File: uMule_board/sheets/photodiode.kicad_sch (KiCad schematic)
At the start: 1 part, among them U1 OPA330xxD

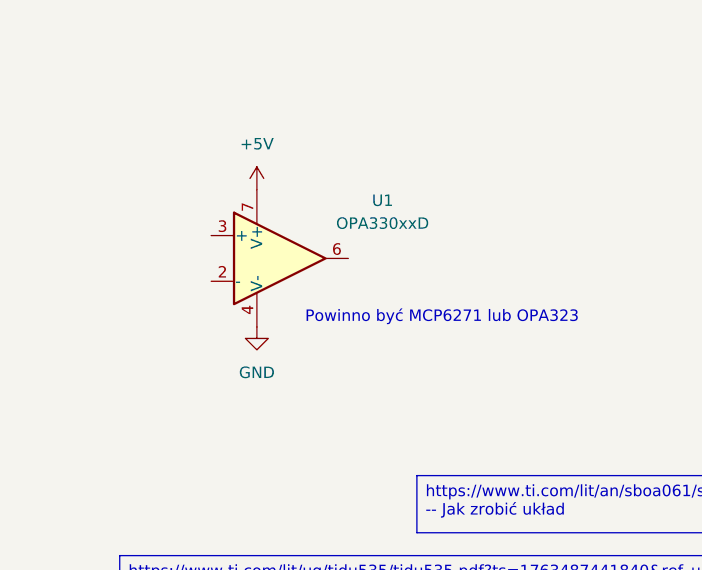
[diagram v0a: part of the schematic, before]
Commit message: addd buses and simple connections
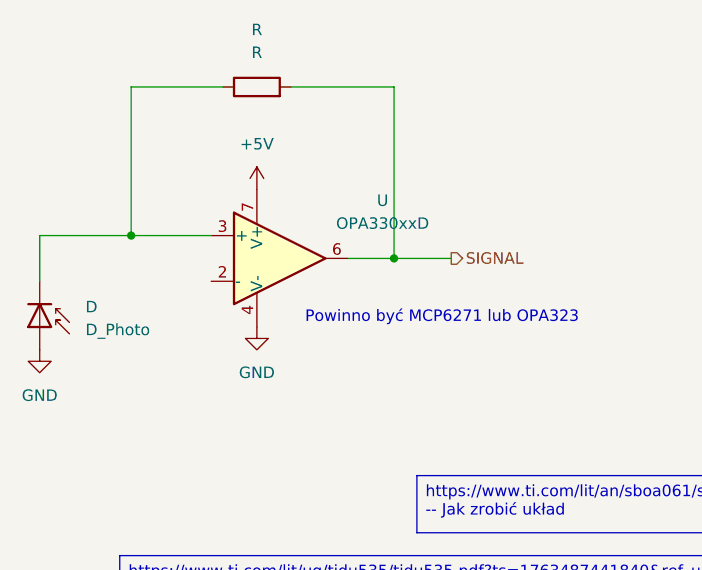
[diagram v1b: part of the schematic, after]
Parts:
- added D: D_Photo, symbol Device:D_Photo
- added R: R, symbol Device:R
- renumbered U1 to U
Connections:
- net GND: now also D.2 (A)
- net at U.3 (+): now also D.1 (K), R.1
- net SIGNAL: now reaches U.6
- net SIGNAL: now also R.2

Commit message: Some calculations were made. Photodiode, amplifier and main procesor are chosen
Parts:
- removed D: D_Photo, symbol Device:D_Photo
- removed U: OPA330xxD, Package_SO:SOIC-8_3.9x4.9mm_P1.27mm, symbol Amplifier_Operational:OPA330xxD
- added P1: BPV10NF, Diode_THT:D_T-1_P2.54mm_Vertical_KathodeUp, symbol My_elemets:BPV10NF
- added R1, R32: R, symbol Device:R
- added U1: OPA397DBVR, Package_TO_SOT_SMD:SOT-23-5, symbol My_elemets:OPA397DBVR
- renumbered R to R12
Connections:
- net GND: now also P1.2 (A), U1.2 (V-)
- net SIGNAL: now also U1.1
- net at R12.1: now also P1.1 (K), U1.4 (-)
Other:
- note added: "IPD = 60uA C = 11pF"
- note added: "Powinno być OPA397DBVR"
- note removed: "Powinno być MCP6271 lub OPA323"

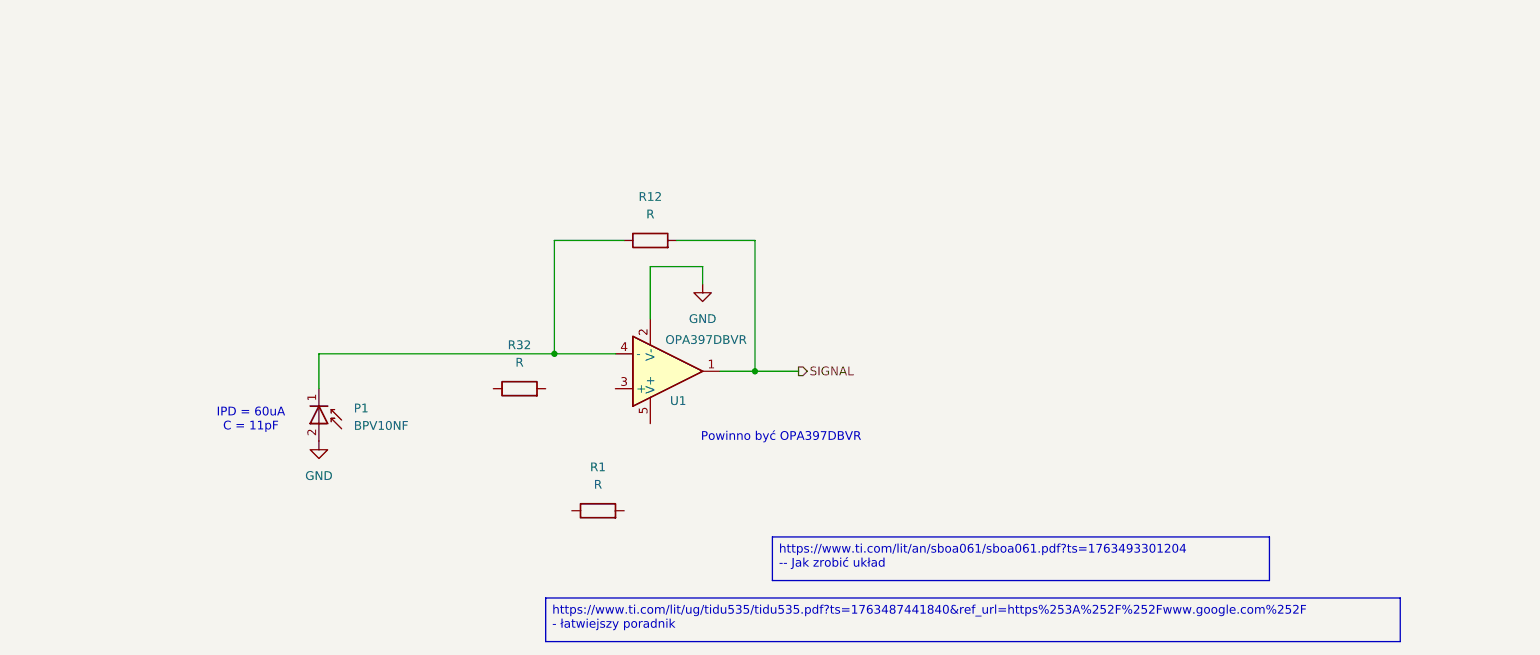
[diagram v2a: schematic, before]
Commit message: all main componenst added. Prepared to change MCU. SCH almost ready
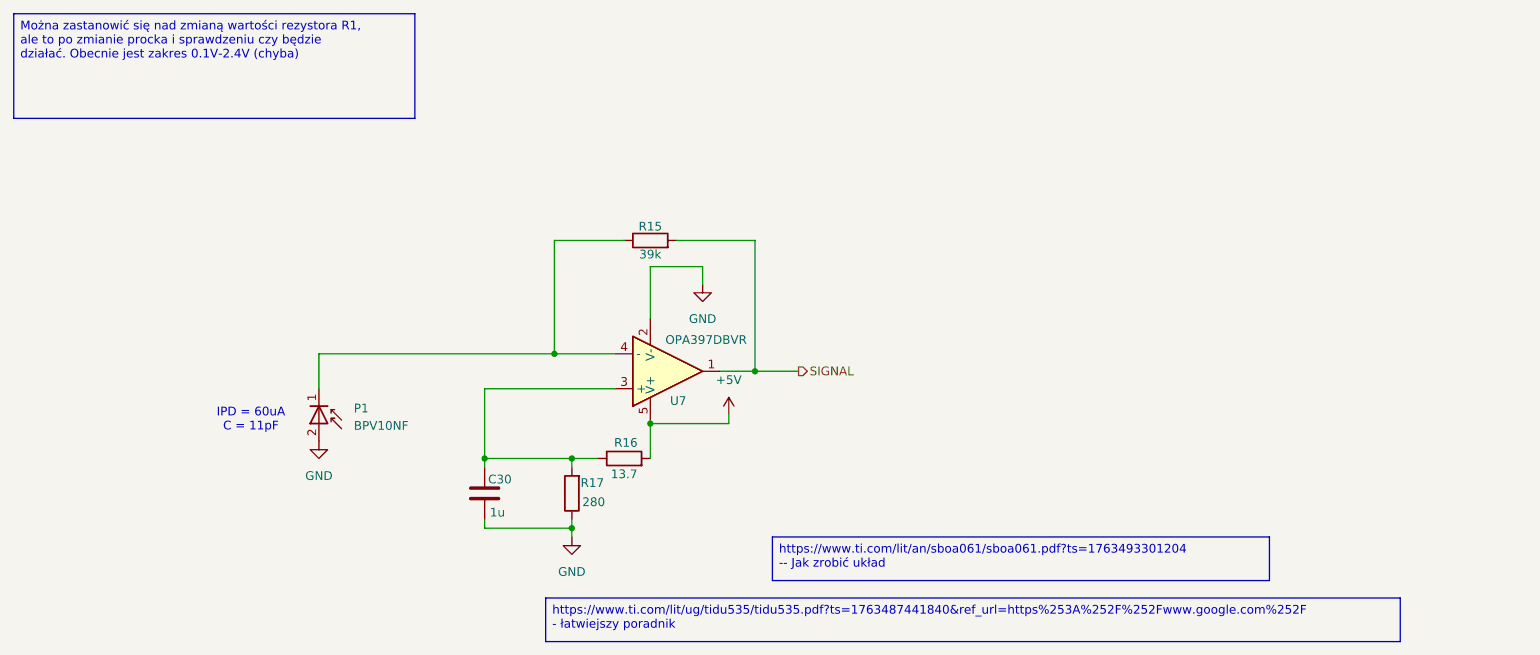
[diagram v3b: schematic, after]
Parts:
- added C30: 1u, Capacitor_SMD:C_0805_2012Metric_Pad1.18x1.45mm_HandSolder, symbol Device:C
- R15: renamed from R12; value R -> 39k
- R16: renamed from R32; value R -> 13.7; footprint (none) -> Resistor_SMD:R_0603_1608Metric_Pad0.98x0.95mm_HandSolder
- R17: renamed from R1; value R -> 280; footprint (none) -> Resistor_SMD:R_0603_1608Metric_Pad0.98x0.95mm_HandSolder
- renumbered U1 to U7
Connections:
- net GND: now also R17.1, C30.2
- net at U7.3 (+): now also R16.1, R17.2, C30.1
- net +5V: now reaches U7.5 (V+)
- net +5V: now also R16.2
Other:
- note removed: "Powinno być OPA397DBVR"
- moved on the sheet: R16, R17

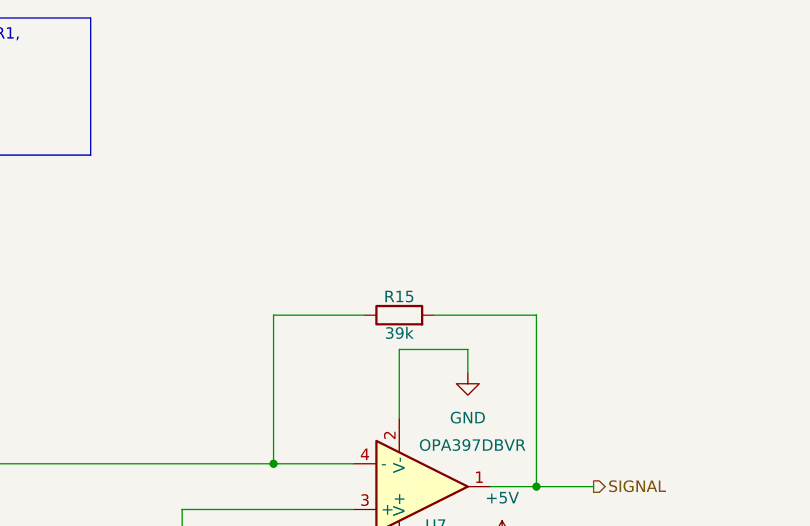
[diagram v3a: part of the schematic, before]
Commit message: Finished schematics. Now ready for PCB
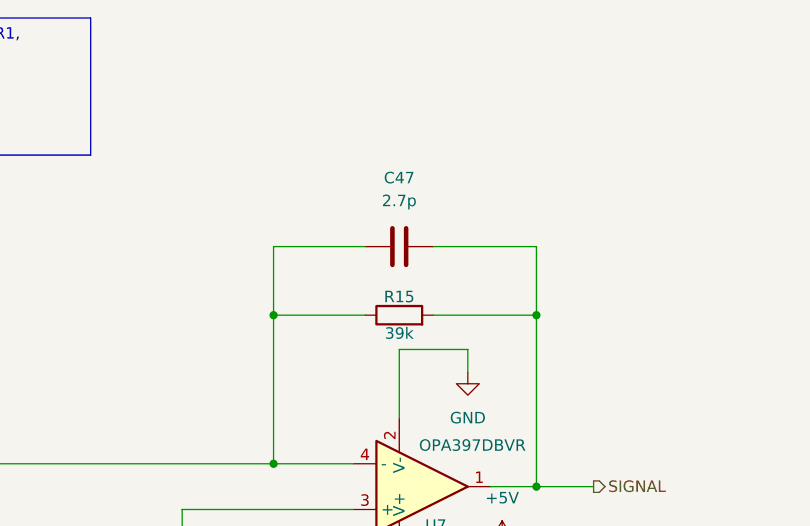
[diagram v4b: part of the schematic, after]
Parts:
- added C47: 2.7p, Capacitor_SMD:C_0603_1608Metric_Pad1.08x0.95mm_HandSolder, symbol Device:C
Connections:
- net SIGNAL: now also C47.2
- net at P1.1 (K), R15.1, U7.4 (-): now also C47.1
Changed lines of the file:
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@@
+	)
+	(junction
+		(at 92.71 46.99)
+		(diameter 0)
+		(color 0 0 0 0)
+	)
+	(junction
+		(at 121.92 46.99)
+		(diameter 0)
+		(color 0 0 0 0)
 	)
 	(junction
@@
 	(wire
 		(pts
+			(xy 102.87 39.37) (xy 92.71 39.37)
+		)
+		(stroke
+			(width 0)
+			(type default)
+		)
+	)
+	(wire
+		(pts
 			(xy 92.71 63.5) (xy 101.6 63.5)
 		)
@@
 	(wire
 		(pts
+			(xy 121.92 39.37) (xy 121.92 46.99)
+		)
+		(stroke
+			(width 0)
+			(type default)
+		)
+	)
+	(wire
+		(pts
 			(xy 106.68 73.66) (xy 118.11 73.66)
 		)
@@
 	(wire
 		(pts
+			(xy 110.49 39.37) (xy 121.92 39.37)
+		)
+		(stroke
+			(width 0)
+			(type default)
+		)
+	)
+	(wire
+		(pts
 			(xy 95.25 90.17) (xy 95.25 88.9)
 		)
@@
 	(wire
 		(pts
+			(xy 92.71 39.37) (xy 92.71 46.99)
+		)
+		(stroke
+			(width 0)
+			(type default)
+		)
+	)
+	(wire
+		(pts
 			(xy 82.55 80.01) (xy 82.55 78.74)
 		)
@@
 	)
 	(image
-		(at 101.6 34.29)
+		(at 105.41 17.78)
 		(scale 1.44752)
 		(data "iVBORw0KGgoAAAANSUhEUgAAAd4AAAAzCAIAAAC2Uf58AAAAA3NCSVQICAjb4U/gAAAd+ElEQVR4"
@@
 		)
 	)
+	(symbol
+		(lib_id "Device:C")
+		(at 106.68 39.37 90)
+		(unit 1)
+		(exclude_from_sim no)
+		(in_bom yes)
+		(on_board yes)
+		(dnp no)
+		(fields_autoplaced yes)
+		(property "Reference" "C47"
+			(at 106.68 31.75 90)
+			(effects
+				(font
+					(size 1.27 1.27)
+				)
+			)
+		)
+		(property "Value" "2.7p"
+			(at 106.68 34.29 90)
+			(effects
+				(font
+					(size 1.27 1.27)
+				)
+			)
+		)
+		(property "Footprint" "Capacitor_SMD:C_0603_1608Metric_Pad1.08x0.95mm_HandSolder"
+			(at 110.49 38.4048 0)
+			(effects
+				(font
+					(size 1.27 1.27)
+				)
+				(hide yes)
+			)
+		)
+		(property "Datasheet" "~"
+			(at 106.68 39.37 0)
+			(effects
+				(font
+					(size 1.27 1.27)
+				)
+				(hide yes)
+			)
+		)
+		(property "Description" "Unpolarized capacitor"
+			(at 106.68 39.37 0)
+			(effects
+				(font
+					(size 1.27 1.27)
+				)
+				(hide yes)
+			)
+		)
+		(pin "1"
+		)
+		(pin "2"
+		)
+		(instances
+			(project ""
+				(path "/3d853824-a92e-40a5-ad1a-5052c8a0bd68/6627633c-9ae5-4253-9ddc-73b5516d7e53/00bfe0a5-cb54-4e03-89d1-fdfae8e2dd96"
+					(reference "C61")
+					(unit 1)
+				)
+				(path "/3d853824-a92e-40a5-ad1a-5052c8a0bd68/6627633c-9ae5-4253-9ddc-73b5516d7e53/183bc9f8-d8c0-49e1-864d-8ec09bfdca1c"
+					(reference "C49")
+					(unit 1)
+				)
+				(path "/3d853824-a92e-40a5-ad1a-5052c8a0bd68/6627633c-9ae5-4253-9ddc-73b5516d7e53/304bf062-9084-4acd-8653-ce29bb447012"
+					(reference "C54")
+					(unit 1)
+				)
+				(path "/3d853824-a92e-40a5-ad1a-5052c8a0bd68/6627633c-9ae5-4253-9ddc-73b5516d7e53/3bb5e9fd-b359-4050-8cd0-6590b1297ba8"
+					(reference "C59")
+					(unit 1)
+				)
+				(path "/3d853824-a92e-40a5-ad1a-5052c8a0bd68/6627633c-9ae5-4253-9ddc-73b5516d7e53/72bba8f0-7459-42e4-9e54-bb4a6b7f89ca"
+					(reference "C55")
+					(unit 1)
+				)
+				(path "/3d853824-a92e-40a5-ad1a-5052c8a0bd68/6627633c-9ae5-4253-9ddc-73b5516d7e53/8248702b-3608-4dff-ae81-31dd06b201dc"
+					(reference "C48")
+					(unit 1)
+				)
+				(path "/3d853824-a92e-40a5-ad1a-5052c8a0bd68/6627633c-9ae5-4253-9ddc-73b5516d7e53/8df3c370-4ee6-4ce1-815f-d4dc8190fa99"
+					(reference "C51")
+					(unit 1)
+				)
+				(path "/3d853824-a92e-40a5-ad1a-5052c8a0bd68/6627633c-9ae5-4253-9ddc-73b5516d7e53/98fc720a-bcce-4344-a0f1-38bf6368bc8b"
+					(reference "C53")
+					(unit 1)
+				)
+				(path "/3d853824-a92e-40a5-ad1a-5052c8a0bd68/6627633c-9ae5-4253-9ddc-73b5516d7e53/9c2366a1-9f21-462d-812f-edfa4dd7df7c"
+					(reference "C60")
+					(unit 1)
+				)
+				(path "/3d853824-a92e-40a5-ad1a-5052c8a0bd68/6627633c-9ae5-4253-9ddc-73b5516d7e53/ac5058d2-8803-44ce-b51c-e668cfeb540d"
+					(reference "C56")
+					(unit 1)
+				)
+				(path "/3d853824-a92e-40a5-ad1a-5052c8a0bd68/6627633c-9ae5-4253-9ddc-73b5516d7e53/bc4d6a90-3c41-4f75-bf34-9f79b7453a8e"
+					(reference "C57")
+					(unit 1)
+				)
+				(path "/3d853824-a92e-40a5-ad1a-5052c8a0bd68/6627633c-9ae5-4253-9ddc-73b5516d7e53/c8ab0fec-f6b3-41ac-aa48-29f38940096b"
+					(reference "C62")
+					(unit 1)
+				)
+				(path "/3d853824-a92e-40a5-ad1a-5052c8a0bd68/6627633c-9ae5-4253-9ddc-73b5516d7e53/c963b1c0-3242-4704-b0d7-ea5d0e867a39"
+					(reference "C52")
+					(unit 1)
+				)
+				(path "/3d853824-a92e-40a5-ad1a-5052c8a0bd68/6627633c-9ae5-4253-9ddc-73b5516d7e53/fb7ea3bf-e8bc-402d-9bd3-991b43c6fe40"
+					(reference "C47")
+					(unit 1)
+				)
+				(path "/3d853824-a92e-40a5-ad1a-5052c8a0bd68/6627633c-9ae5-4253-9ddc-73b5516d7e53/fe64fe54-7dc5-480a-8e9b-552cfa7155af"
+					(reference "C58")
+					(unit 1)
+				)
+				(path "/3d853824-a92e-40a5-ad1a-5052c8a0bd68/6627633c-9ae5-4253-9ddc-73b5516d7e53/ff046bcc-0ecf-4438-b231-ef090549f4b5"
+					(reference "C50")
+					(unit 1)
+				)
+			)
+		)
+	)

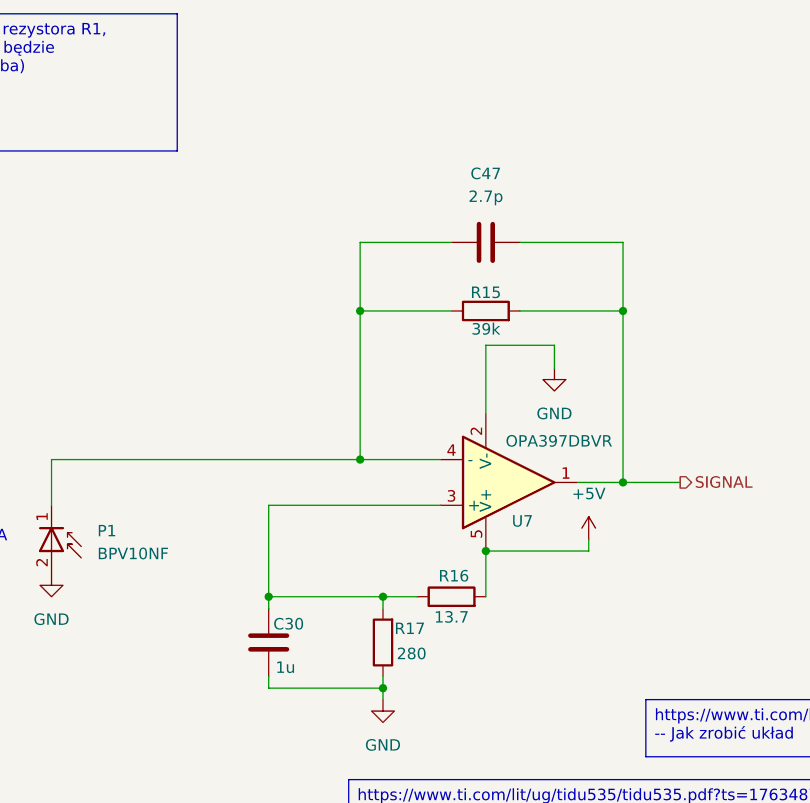
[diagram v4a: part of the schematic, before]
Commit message: Started working on PCB. Ditched high power outputs. Focusing on photodiodes. One commit closer to order
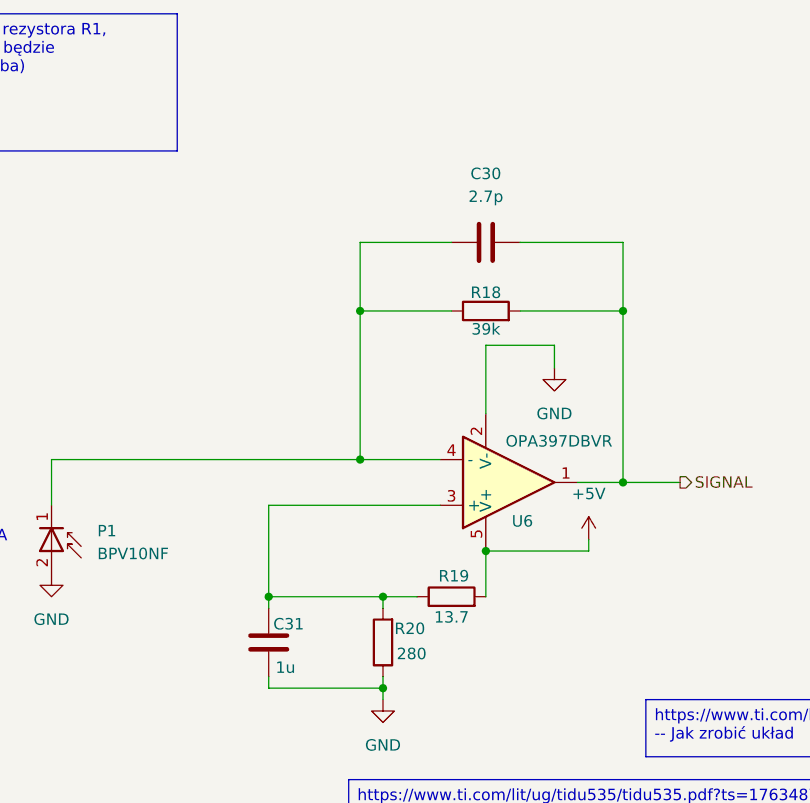
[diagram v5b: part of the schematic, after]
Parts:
- C30: renamed from C47; footprint Capacitor_SMD:C_0603_1608Metric_Pad1.08x0.95mm_HandSolder -> Capacitor_SMD:C_0402_1005Metric
- R18: renamed from R15; footprint (none) -> Resistor_SMD:R_0603_1608Metric
- renumbered C30 to C31, R16 to R19, R17 to R20, U7 to U6
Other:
- title: (none) -> uMule_board

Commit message: sch ready, only missing the pcb
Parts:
- removed C31: 1u, Capacitor_SMD:C_0805_2012Metric_Pad1.18x1.45mm_HandSolder, symbol Device:C
- removed R19: 13.7, Resistor_SMD:R_0603_1608Metric_Pad0.98x0.95mm_HandSolder, symbol Device:R
- removed R20: 280, Resistor_SMD:R_0603_1608Metric_Pad0.98x0.95mm_HandSolder, symbol Device:R
- renumbered C30 to C41, R18 to R27, U6 to U8
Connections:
- net GND: no longer U8.2 (V-)
- net V_{REF}: now reaches U8.3 (+)
- new net -5V: U8.2 (V-)
